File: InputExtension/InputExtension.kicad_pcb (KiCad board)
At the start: 2 copper layers, 10 parts, among them P1 CONN_01X04, P2 CONN_01X04, P3 CONN_01X08, P4 CONN_01X08, U1 PCF8574

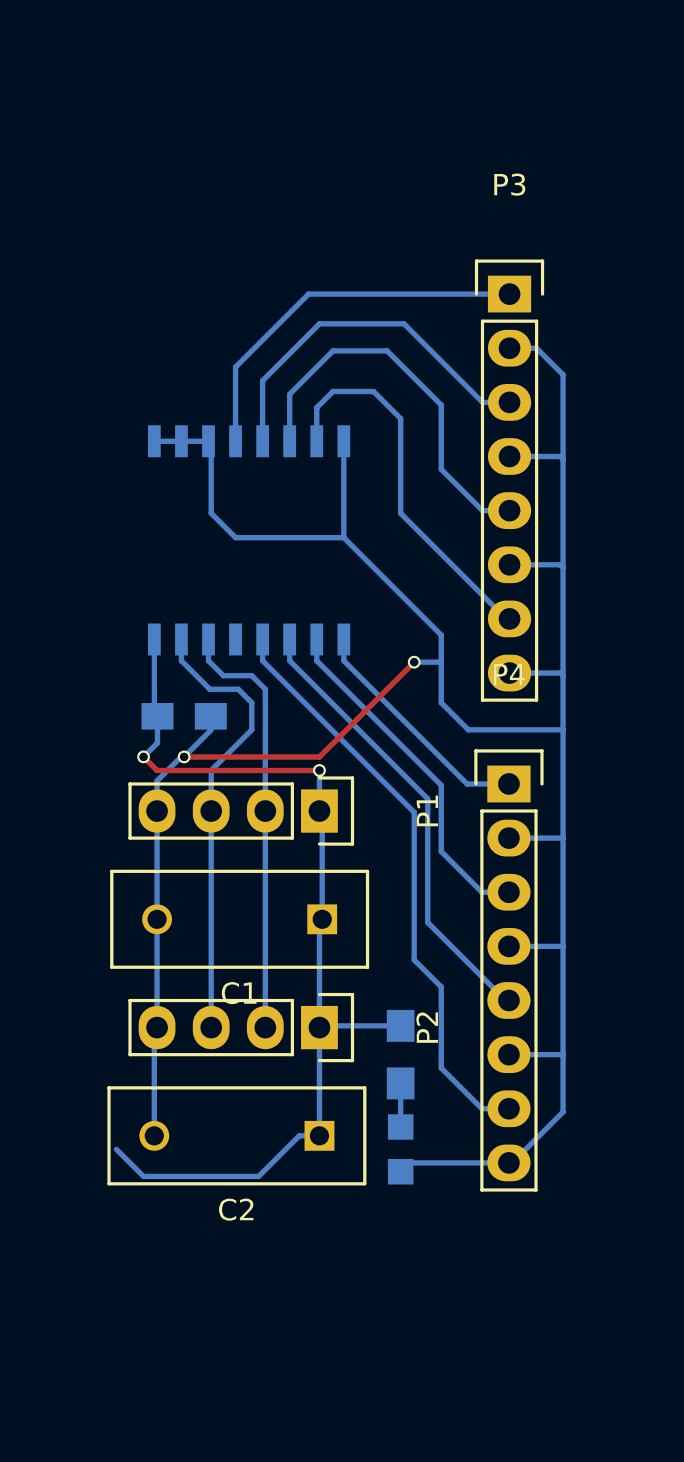
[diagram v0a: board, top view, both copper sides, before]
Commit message: Added the Input extension PCB layout
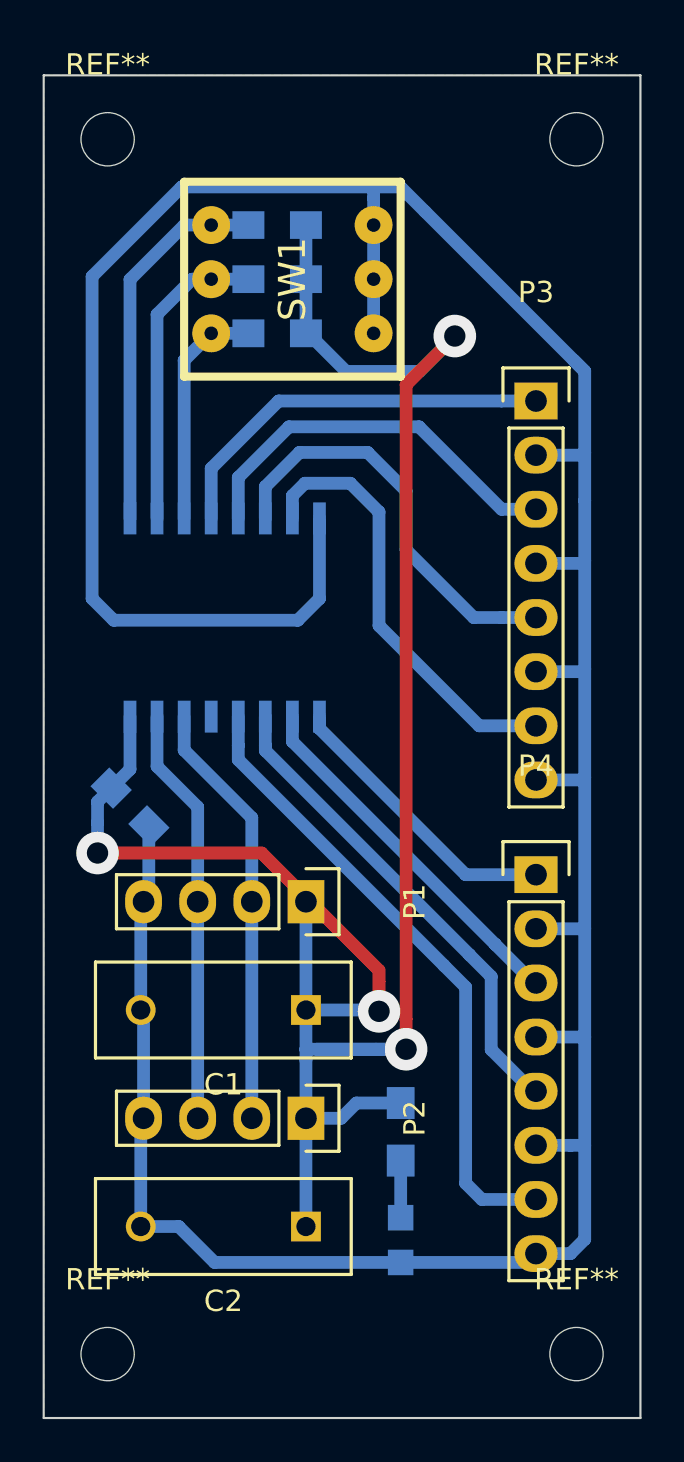
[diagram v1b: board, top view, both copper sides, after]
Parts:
- added R2: R, Resistors_SMD:R_0805_HandSoldering, B.Cu at (153.0, 69.0)
- added R3: R, Resistors_SMD:R_0805_HandSoldering, B.Cu at (153.0, 71.6)
- added R4: R, Resistors_SMD:R_0805_HandSoldering, B.Cu at (153.0, 74.1)
- added REF**: MountingHole_2-5mm, Mounting_Holes:MountingHole_2-5mm, F.Cu at (145.0, 122.0)
- added REF**: MountingHole_2-5mm, Mounting_Holes:MountingHole_2-5mm, F.Cu at (167.0, 122.0)
- added REF**: MountingHole_2-5mm, Mounting_Holes:MountingHole_2-5mm, F.Cu at (167.0, 65.0)
- added REF**: MountingHole_2-5mm, Mounting_Holes:MountingHole_2-5mm, F.Cu at (145.0, 65.0)
- added SW1: DIPS_03, dips-s:DIPS-DS03, F.Cu at (153.7, 71.6)
- moved P3 5.17 mm to (165.1, 77.3)
- moved C3 4.96 mm to (146.1, 96.3), turned to 315 degrees
- moved P4 4.44 mm to (165.1, 99.5)
- moved C1 4.32 mm to (154.3, 105.9)
- moved P1 4.30 mm to (154.3, 100.8)
- moved C2 4.30 mm to (154.3, 116.0)
- moved P2 4.30 mm to (154.3, 110.9)
- moved D1 4.26 mm to (158.8, 116.7)
- moved U1 3.80 mm to (150.5, 87.4)
- moved R1 3.62 mm to (158.8, 111.6)
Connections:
- U1 pad 1: GND -> Net-(R2-Pad2)
- U1 pad 13: (no net) -> Net-(U1-Pad13)
- U1 pad 2: GND -> Net-(R3-Pad2)
- U1 pad 3: GND -> Net-(R4-Pad2)
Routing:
- net +5V: track 46.5 -> 105.3 mm, vias 2 -> 4
- net GND: track 129.9 -> 164.5 mm, vias 2 -> 0
- net Net-(R2-Pad2): track 0.00 -> 17.8 mm
- net Net-(R3-Pad2): track 0.00 -> 14.5 mm
- net Net-(R4-Pad2): track 0.00 -> 11.0 mm
- net Net-(P3-Pad7): track 18.0 -> 20.6 mm
- net Net-(P4-Pad7): track 27.5 -> 29.9 mm
- net Net-(P4-Pad1): track 11.3 -> 13.6 mm
- net /I2C_SDA: track 21.6 -> 19.6 mm
- net Net-(P4-Pad5): track 21.3 -> 22.9 mm
- net Net-(P3-Pad5): track 18.2 -> 19.7 mm
- net Net-(P3-Pad3): track 17.1 -> 18.5 mm
- net Net-(P3-Pad1): track 17.8 -> 18.9 mm
- net Net-(P4-Pad3): track 16.3 -> 17.3 mm
- net Net-(D1-Pad2): track 2.05 -> 2.68 mm
- added copper zone on B.Cu, net GND
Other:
- board outline added: 28 x 63 mm
- net class Default: clearance 0.2 -> 0.6; trace_width 0.25 -> 0.6; via_dia 0.6 -> 2; via_drill 0.4 -> 1
- rule trace_clearance: 0.2 -> 0.6
- rule trace_min: 0.2 -> 0.6
- rule via_min_drill: 0.3 -> 1
- rule via_min_size: 0.4 -> 1.3

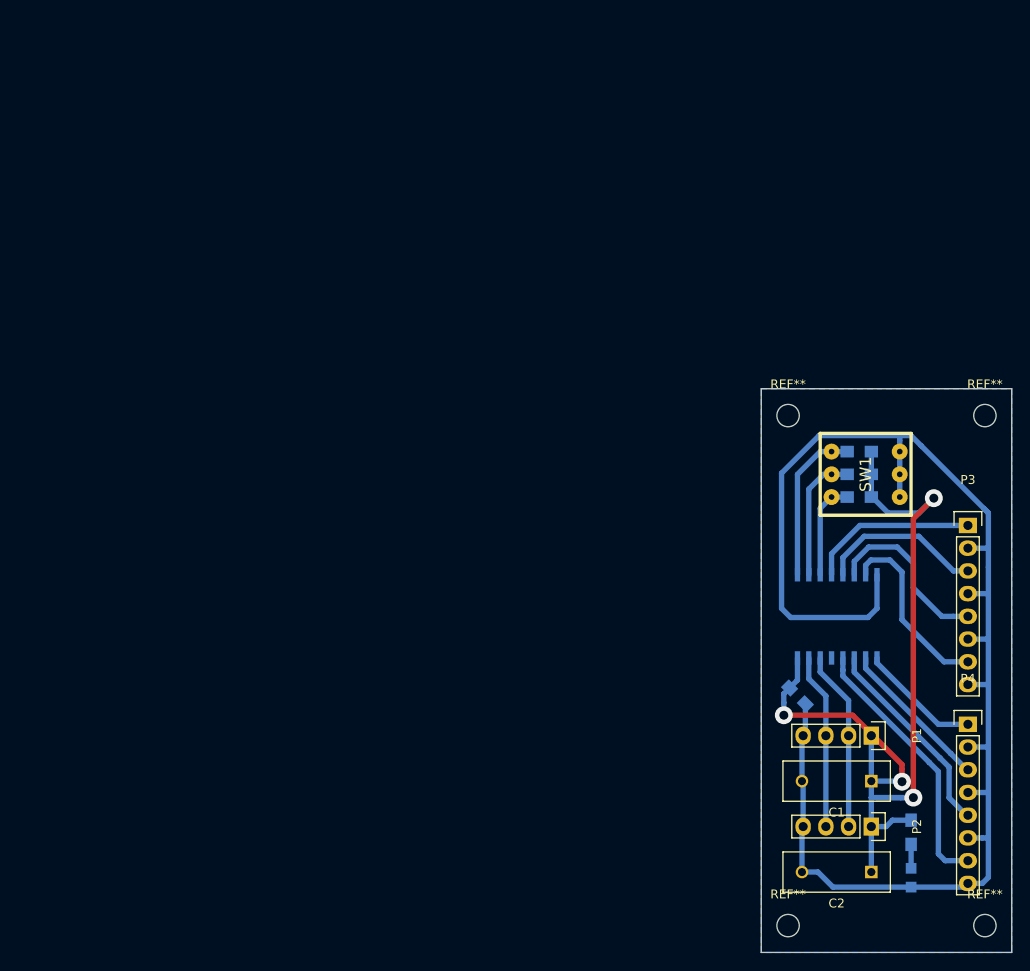
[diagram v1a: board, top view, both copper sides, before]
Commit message: Add new input extension pcb
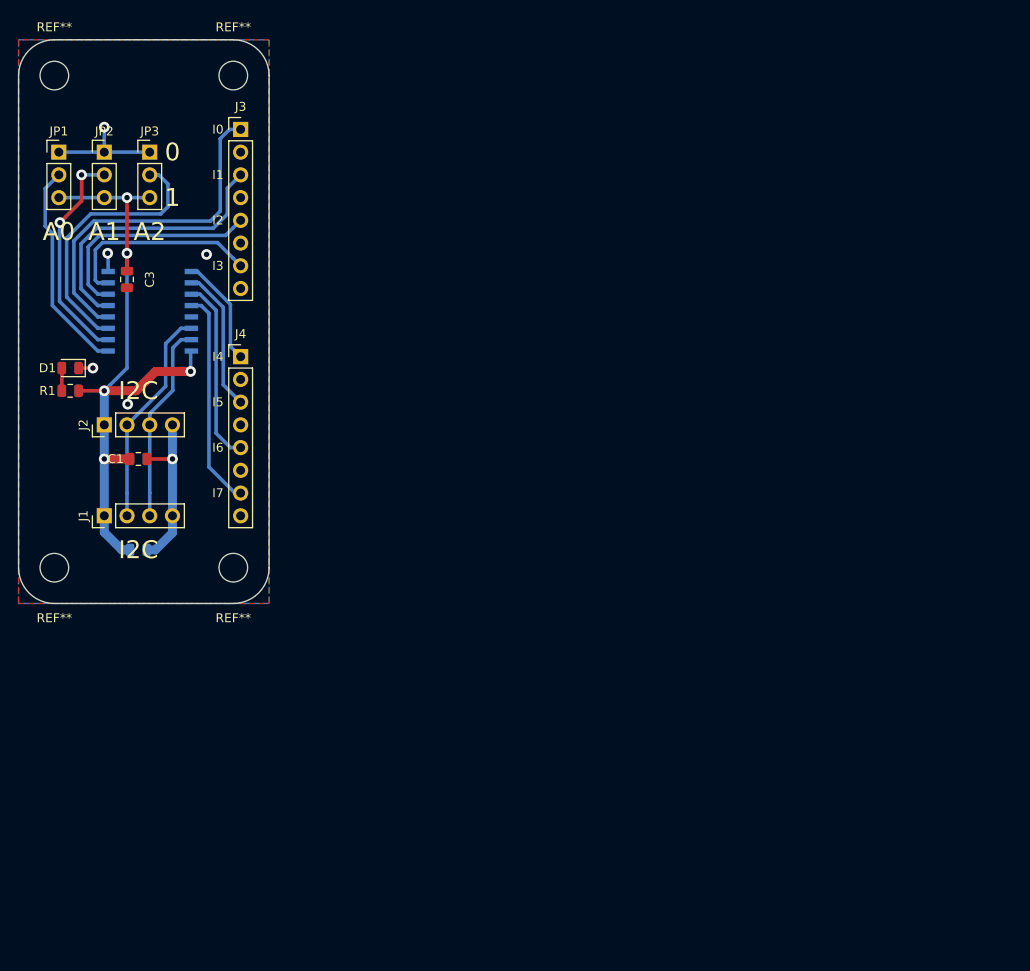
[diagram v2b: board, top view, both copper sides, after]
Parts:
- removed P1, P2: CONN_01X04, Pin_Headers:Pin_Header_Straight_1x04
- removed P3, P4: CONN_01X08, Pin_Headers:Pin_Header_Straight_1x08
- removed R2, R3, R4: R, Resistors_SMD:R_0805_HandSoldering
- removed the REF** at (145.0, 122.0)
- removed the REF** at (167.0, 122.0)
- removed the REF** at (167.0, 65.0)
- removed the REF** at (145.0, 65.0)
- removed SW1: DIPS_03, dips-s:DIPS-DS03
- added J1: Conn_01x04, Connector_PinHeader_2.54mm:PinHeader_1x04_P2.54mm_Vertical, F.Cu at (68.6, 76.2)
- added J2: Conn_01x04, Connector_PinHeader_2.54mm:PinHeader_1x04_P2.54mm_Vertical, F.Cu at (68.6, 66.0)
- added J3: Conn_01x08, Connector_PinHeader_2.54mm:PinHeader_1x08_P2.54mm_Vertical, F.Cu at (83.8, 33.0)
- added J4: Conn_01x08, Connector_PinHeader_2.54mm:PinHeader_1x08_P2.54mm_Vertical, F.Cu at (83.8, 58.4)
- added JP1: JP, Connector_PinHeader_2.54mm:PinHeader_1x03_P2.54mm_Vertical, F.Cu at (63.5, 35.6)
- added JP2: JP, Connector_PinHeader_2.54mm:PinHeader_1x03_P2.54mm_Vertical, F.Cu at (68.6, 35.6)
- added JP3: JP, Connector_PinHeader_2.54mm:PinHeader_1x03_P2.54mm_Vertical, F.Cu at (73.7, 35.6)
- added REF**: MountingHole_3.2mm_M3, MountingHole:MountingHole_3.2mm_M3, F.Cu at (63.0, 27.0)
- added REF**: MountingHole_3.2mm_M3, MountingHole:MountingHole_3.2mm_M3, F.Cu at (83.0, 27.0)
- added REF**: MountingHole_3.2mm_M3, MountingHole:MountingHole_3.2mm_M3, F.Cu at (83.0, 82.0)
- added REF**: MountingHole_3.2mm_M3, MountingHole:MountingHole_3.2mm_M3, F.Cu at (63.0, 82.0)
- C1: value 100n -> 1u; footprint Capacitors_ThroughHole:C_Disc_D12_P7.75 -> Capacitor_SMD:C_0805_2012Metric
- C2: value 100n -> 1u; footprint Capacitors_ThroughHole:C_Disc_D12_P7.75 -> Capacitor_SMD:C_0805_2012Metric; moved to B.Cu
- C3: value 100n -> 1u; footprint Capacitors_SMD:C_0805_HandSoldering -> Capacitor_SMD:C_0805_2012Metric; moved to F.Cu
- D1: footprint LEDs:LED-0805 -> LED_SMD:LED_0805_2012Metric; moved to F.Cu
- R1: value 220 -> 220R; footprint Resistors_SMD:R_0805_HandSoldering -> Resistor_SMD:R_0805_2012Metric; moved to F.Cu
- U1: footprint Housings_SOIC:SOIC-16_7.5x10.3mm_Pitch1.27mm -> Package_SO:SOIC-16W_7.5x10.3mm_P1.27mm
- moved D1 109.9 mm to (64.8, 59.7), turned to 180 degrees
- moved R1 106.1 mm to (64.8, 62.2), turned to 180 degrees
- moved C1 89.5 mm to (72.4, 69.8), turned to 0 degrees
- moved C2 89.5 mm to (72.4, 80.0), turned to 0 degrees
- moved C3 88.2 mm to (71.1, 49.8), turned to 270 degrees
- moved U1 84.1 mm to (73.7, 53.3), turned to 0 degrees
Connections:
- R1 pad 1: Net-(D1-Pad2) -> +5V
- R1 pad 2: +5V -> Net-(D1-Pad2)
- U1 pad 1: Net-(R2-Pad2) -> /A0
- U1 pad 2: Net-(R3-Pad2) -> /A1
- U1 pad 3: Net-(R4-Pad2) -> /A2
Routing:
- net GND: track 164.5 -> 35.2 mm, vias 0 -> 6
- net +5V: track 105.3 -> 74.3 mm, vias 4 -> 5
- net /A2: track 0.00 -> 30.4 mm
- net /A1: track 0.00 -> 24.9 mm, vias 0 -> 2
- net /A0: track 0.00 -> 23.9 mm
- net Net-(J3-Pad1): track 18.9 -> 39.3 mm
- net Net-(R2-Pad2): track 17.8 -> 0.00 mm
- net Net-(R3-Pad2): track 14.5 -> 0.00 mm
- net Net-(J3-Pad3): track 18.5 -> 31.6 mm
- net Net-(R4-Pad2): track 11.0 -> 0.00 mm
- net Net-(J4-Pad7): track 29.9 -> 24.3 mm
- net Net-(J3-Pad5): track 19.7 -> 25.2 mm
- net /I2C_SCL: track 20.2 -> 24.6 mm
- net /I2C_SDA: track 19.6 -> 22.3 mm
- net Net-(J4-Pad5): track 22.9 -> 20.7 mm
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- added copper zone on F.Cu, net GND
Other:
- outline, holes or cut-outs redrawn
- net class Default: clearance 0.6 -> 0.4; trace_width 0.6 -> 0.4; via_dia 2 -> 1.2; via_drill 1 -> 0.6
- rule pad_to_mask_clearance: 0 -> 0.051
- rule trace_clearance: 0.6 -> 0.4
- rule trace_min: 0.6 -> 0.4
- rule via_min_drill: 1 -> 0.6
- rule via_min_size: 1.3 -> 1.2
- board text added: "0"
- board text added: "1"
- board text added: "A0"
- board text added: "A1"
- board text added: "A2"
- board text added: "I0"
- board text added: "I1"
- board text added: "I2"
- board text added: "I2C"
- board text added: "I3"
- board text added: "I4"
- board text added: "I5"
- board text added: "I6"
- board text added: "I7"

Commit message: silkscreen
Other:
- board text added: "Fan-Tas-Tic"
- board text added: "GND"
- board text added: "input extension"
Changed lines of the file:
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@@
-(kicad_pcb (version 20171130) (host pcbnew 6.0.0-rc1-unknown-7dfc4e3~65~ubuntu18.04.1)
+(kicad_pcb (version 20171130) (host pcbnew "(5.0.1-34-g9610f8f20)")
   (general
     (thickness 1.6)
-    (drawings 23)
+    (drawings 33)
     (tracks 139)
     (zones 0)
@@
     (zone_45_only no)
     (trace_min 0.4)
+    (segment_width 0.2)
+    (edge_width 0.15)
     (via_size 1.2)
     (via_drill 0.6)
@@
     (uvia_min_size 0.2)
     (uvia_min_drill 0.1)
-    (edge_width 0.15)
-    (segment_width 0.2)
     (pcb_text_width 0.3)
     (pcb_text_size 1.5 1.5)
@@
     (uvia_dia 0.3)
     (uvia_drill 0.1)
+    (diff_pair_gap 0.4)
     (diff_pair_width 0.4)
-    (diff_pair_gap 0.4)
     (add_net +5V)
     (add_net /A0)
@@
     (tags capacitor)
     (attr smd)
-    (fp_text reference C3 (at 0 -2.54 270) (layer F.SilkS)
+    (fp_text reference C3 (at -0.254 -2.54) (layer F.SilkS)
       (effects (font (size 1 1) (thickness 0.15)))
     )
@@
     (pad 1 np_thru_hole circle (at 0 0) (size 3.2 3.2) (drill 3.2) (layers *.Cu *.Mask))
   )
+  (gr_text GND (at 81.28 76.2) (layer F.SilkS)
+    (effects (font (size 1 1) (thickness 0.15)) (justify right))
+  )
+  (gr_text GND (at 81.28 71.12) (layer F.SilkS)
+    (effects (font (size 1 1) (thickness 0.15)) (justify right))
+  )
+  (gr_text GND (at 81.28 66.04) (layer F.SilkS)
+    (effects (font (size 1 1) (thickness 0.15)) (justify right))
+  )
+  (gr_text GND (at 81.28 60.96) (layer F.SilkS)
+    (effects (font (size 1 1) (thickness 0.15)) (justify right))
+  )
+  (gr_text GND (at 81.28 50.8) (layer F.SilkS)
+    (effects (font (size 1 1) (thickness 0.15)) (justify right))
+  )
+  (gr_text GND (at 81.28 45.72) (layer F.SilkS)
+    (effects (font (size 1 1) (thickness 0.15)) (justify right))
+  )
+  (gr_text GND (at 81.28 40.64) (layer F.SilkS)
+    (effects (font (size 1 1) (thickness 0.15)) (justify right))
+  )
+  (gr_text GND (at 81.28 35.56) (layer F.SilkS)
+    (effects (font (size 1 1) (thickness 0.15)) (justify right))
+  )
+  (gr_text "input extension" (at 71.12 56.642) (layer F.SilkS)
+    (effects (font (size 1 1) (thickness 0.2) italic))
+  )
+  (gr_text Fan-Tas-Tic (at 70.739 54.229) (layer F.SilkS)
+    (effects (font (size 2 2) (thickness 0.4)))
+  )
   (gr_text I7 (at 81.28 73.66) (layer F.SilkS)
-    (effects (font (size 1 1) (thickness 0.15)))
+    (effects (font (size 1 1) (thickness 0.15)) (justify right))
   )
   (gr_text I6 (at 81.28 68.58) (layer F.SilkS)
-    (effects (font (size 1 1) (thickness 0.15)))
+    (effects (font (size 1 1) (thickness 0.15)) (justify right))
   )
   (gr_text I5 (at 81.28 63.5) (layer F.SilkS)
-    (effects (font (size 1 1) (thickness 0.15)))
+    (effects (font (size 1 1) (thickness 0.15)) (justify right))
   )
   (gr_text I4 (at 81.28 58.42) (layer F.SilkS)
-    (effects (font (size 1 1) (thickness 0.15)))
+    (effects (font (size 1 1) (thickness 0.15)) (justify right))
   )
   (gr_text I3 (at 81.28 48.26) (layer F.SilkS)
-    (effects (font (size 1 1) (thickness 0.15)))
+    (effects (font (size 1 1) (thickness 0.15)) (justify right))
   )
   (gr_text I2 (at 81.28 43.18) (layer F.SilkS)
-    (effects (font (size 1 1) (thickness 0.15)))
+    (effects (font (size 1 1) (thickness 0.15)) (justify right))
   )
   (gr_text I1 (at 81.28 38.1) (layer F.SilkS)
-    (effects (font (size 1 1) (thickness 0.15)))
+    (effects (font (size 1 1) (thickness 0.15)) (justify right))
   )
   (gr_text I0 (at 81.28 33.02) (layer F.SilkS)
-    (effects (font (size 1 1) (thickness 0.15)))
+    (effects (font (size 1 1) (thickness 0.15)) (justify right))
   )
   (gr_text 1 (at 76.2 40.64) (layer F.SilkS)
